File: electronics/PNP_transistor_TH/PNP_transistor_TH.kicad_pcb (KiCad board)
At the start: 2 copper layers, 19 x 19 mm, 7 parts, among them J1 B, J2 E, J3 C, J4 E, Q1 BC547

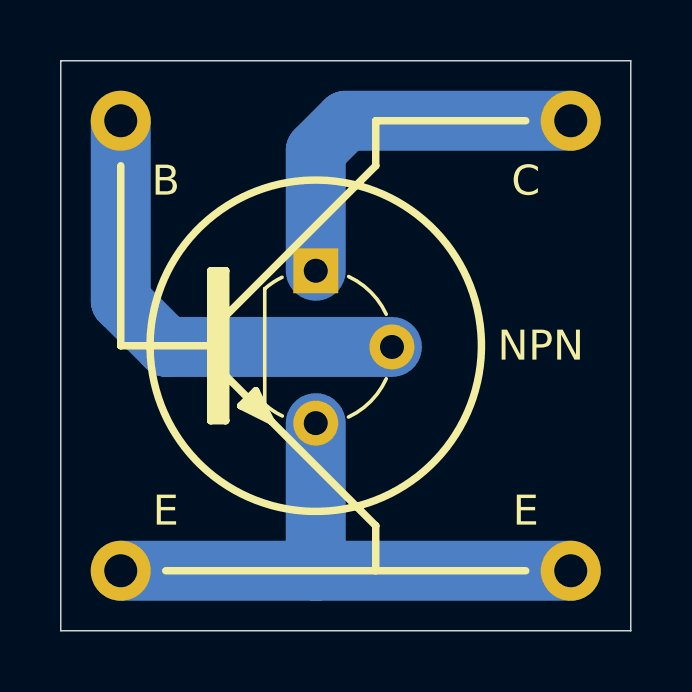
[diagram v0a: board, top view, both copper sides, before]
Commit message: final changes to PNP transistor
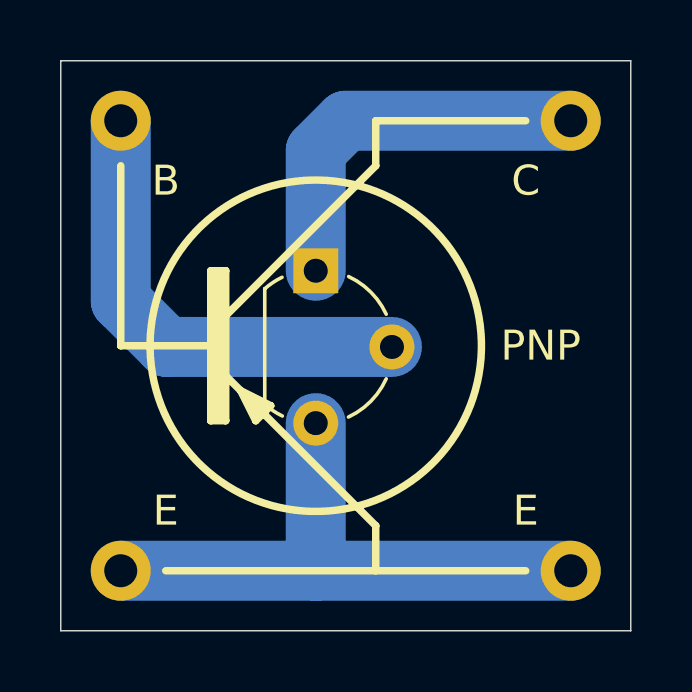
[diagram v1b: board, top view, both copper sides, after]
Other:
- board text added: "PNP"
- board text removed: "NPN"
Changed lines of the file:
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@@
   )
   (setup
-    (last_trace_width 2)
+    (last_trace_width 0.25)
     (user_trace_width 0.2)
     (user_trace_width 0.3)
@@
       (effects (font (size 1 1) (thickness 0.15)))
     )
+    (fp_line (start 0.65 1.6) (end 4.4 1.6) (layer F.Fab) (width 0.1))
+    (fp_line (start 0.6 1.7) (end 4.45 1.7) (layer F.SilkS) (width 0.12))
+    (fp_line (start -1 1.85) (end 6.1 1.85) (layer B.CrtYd) (width 0.05))
+    (fp_line (start 6.1 1.85) (end 6.1 -3.55) (layer B.CrtYd) (width 0.05))
+    (fp_line (start 6.1 -3.55) (end -1 -3.55) (layer B.CrtYd) (width 0.05))
+    (fp_line (start -1 -3.55) (end -1 1.85) (layer B.CrtYd) (width 0.05))
     (fp_arc (start 2.54 0) (end 4.45 1.7) (angle -15.88591585) (layer F.SilkS) (width 0.12))
     (fp_arc (start 2.54 0) (end 2.54 -2.48) (angle -130.2499344) (layer F.Fab) (width 0.1))
@@
       (effects (font (size 1 1) (thickness 0.15)))
     )
-    (fp_line (start -1 -3.55) (end -1 1.85) (layer B.CrtYd) (width 0.05))
-    (fp_line (start 6.1 -3.55) (end -1 -3.55) (layer B.CrtYd) (width 0.05))
-    (fp_line (start 6.1 1.85) (end 6.1 -3.55) (layer B.CrtYd) (width 0.05))
-    (fp_line (start -1 1.85) (end 6.1 1.85) (layer B.CrtYd) (width 0.05))
-    (fp_line (start 0.6 1.7) (end 4.45 1.7) (layer F.SilkS) (width 0.12))
-    (fp_line (start 0.65 1.6) (end 4.4 1.6) (layer F.Fab) (width 0.1))
     (pad 1 thru_hole rect (at 0 0 270) (size 1.5 1.5) (drill 0.8) (layers *.Cu *.Mask)
       (net 3 "Net-(J3-Pad1)"))
@@
       (effects (font (size 1 1) (thickness 0.15)))
     )
+    (fp_circle (center 0 0) (end 1.3 0) (layer F.CrtYd) (width 0.025))
     (fp_circle (center 0 0) (end 1.3 0) (layer B.CrtYd) (width 0.025))
-    (fp_circle (center 0 0) (end 1.3 0) (layer F.CrtYd) (width 0.025))
     (pad 1 thru_hole circle (at 0 0) (size 2 2) (drill 1.1) (layers *.Cu *.Mask)
       (net 2 "Net-(J2-Pad1)"))
@@
       (effects (font (size 1 1) (thickness 0.15)))
     )
+    (fp_circle (center 0 0) (end 1.3 0) (layer F.CrtYd) (width 0.025))
     (fp_circle (center 0 0) (end 1.3 0) (layer B.CrtYd) (width 0.025))
-    (fp_circle (center 0 0) (end 1.3 0) (layer F.CrtYd) (width 0.025))
     (pad 1 thru_hole circle (at 0 0) (size 2 2) (drill 1.1) (layers *.Cu *.Mask)
       (net 3 "Net-(J3-Pad1)"))
@@
       (effects (font (size 1 1) (thickness 0.15)))
     )
+    (fp_circle (center 0 0) (end 1.3 0) (layer F.CrtYd) (width 0.025))
     (fp_circle (center 0 0) (end 1.3 0) (layer B.CrtYd) (width 0.025))
-    (fp_circle (center 0 0) (end 1.3 0) (layer F.CrtYd) (width 0.025))
     (pad 1 thru_hole circle (at 0 0) (size 2 2) (drill 1.1) (layers *.Cu *.Mask)
       (net 2 "Net-(J2-Pad1)"))
@@
       (effects (font (size 1 1) (thickness 0.15)))
     )
+    (fp_circle (center 0 0) (end 1.3 0) (layer F.CrtYd) (width 0.025))
     (fp_circle (center 0 0) (end 1.3 0) (layer B.CrtYd) (width 0.025))
-    (fp_circle (center 0 0) (end 1.3 0) (layer F.CrtYd) (width 0.025))
     (pad 1 thru_hole circle (at 0 0) (size 2 2) (drill 1.1) (layers *.Cu *.Mask)
       (net 1 "Net-(J1-Pad1)"))
@@
     (fp_line (start -0.5 -0.6) (end 0.5 -0.6) (layer B.SilkS) (width 0.15))
   )
-  (gr_poly (pts (xy 147 73) (xy 146 72.5) (xy 146.5 72)) (layer F.SilkS) (width 0.1))
+  (gr_poly (pts (xy 147 72.5) (xy 146.5 73) (xy 146 72)) (layer F.SilkS) (width 0.1))
+  (gr_line (start 146.5 73) (end 146 72) (layer F.SilkS) (width 0.25))
+  (gr_line (start 147 72.5) (end 146.5 73) (layer F.SilkS) (width 0.25))
+  (gr_line (start 146 72) (end 147 72.5) (layer F.SilkS) (width 0.25))
   (gr_poly (pts (xy 145.5 73) (xy 145 73) (xy 145 68) (xy 145.5 68)) (layer F.SilkS) (width 0.1))
-  (gr_line (start 146 72.5) (end 147 73) (layer F.SilkS) (width 0.25))
-  (gr_line (start 146.5 72) (end 146 72.5) (layer F.SilkS) (width 0.25))
-  (gr_line (start 147 73) (end 146.5 72) (layer F.SilkS) (width 0.25))
   (gr_line (start 150.5 63) (end 155.5 63) (layer F.SilkS) (width 0.25))
   (gr_line (start 150.5 64.5) (end 150.5 63) (layer F.SilkS) (width 0.25))
@@
   (gr_line (start 142 70.5) (end 145 70.5) (layer F.SilkS) (width 0.25))
   (gr_line (start 142 64.5) (end 142 70.5) (layer F.SilkS) (width 0.25))
-  (gr_text NPN (at 156 70.5) (layer F.SilkS)
+  (gr_text PNP (at 156 70.5) (layer F.SilkS)
     (effects (font (size 1 1) (thickness 0.15)))
   )

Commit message: small fixes to PNP transistor module
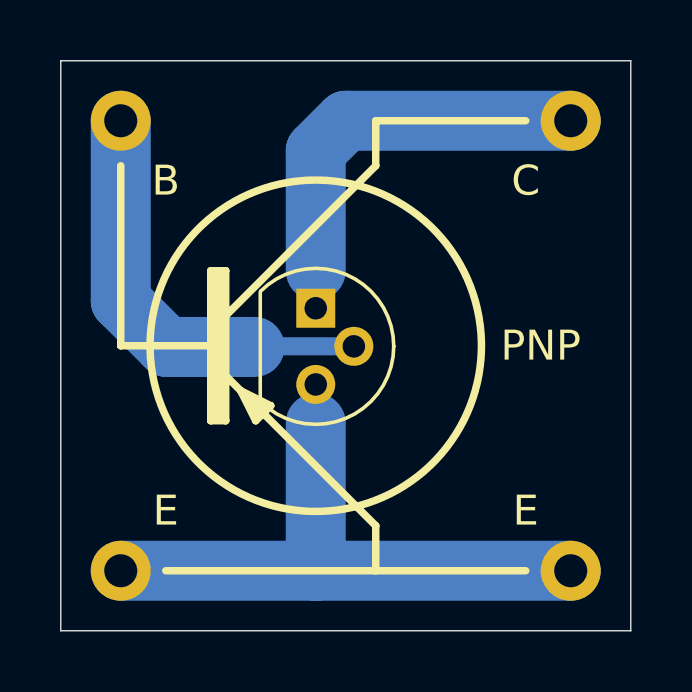
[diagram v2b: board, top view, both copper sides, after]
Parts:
- N1: value 20201118 -> V20201122
- Q1: footprint Package_TO_SOT_THT:TO-92L_Wide -> Package_TO_SOT_THT:TO-92
- moved N1 16.3 mm to (157.8, 71.2)
- moved N2 1.50 mm to (154.0, 70.5)
- moved Q1 1.25 mm to (148.5, 69.2)
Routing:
- net Net-(J2-Pad1): track 19.9 -> 21.2 mm
- net Net-(J1-Pad1): track 15.7 -> 14.4 mm
- net Net-(J3-Pad1): track 12.9 -> 14.2 mm
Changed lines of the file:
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@@
     (thickness 1.6)
     (drawings 24)
-    (tracks 9)
+    (tracks 13)
     (zones 0)
     (modules 7)
@@
   )
   (setup
-    (last_trace_width 0.25)
+    (last_trace_width 0.6)
     (user_trace_width 0.2)
     (user_trace_width 0.3)
@@
     (add_net "Net-(J3-Pad1)")
   )
-  (module Package_TO_SOT_THT:TO-92L_Wide (layer F.Cu)
-    (at 148.5 68 270)
-    (descr "TO-92L leads in-line (large body variant of TO-92), also known as TO-226, wide, drill 0.75mm (see https://www.diodes.com/assets/Package-Files/TO92L.pdf and http://www.ti.com/lit/an/snoa059/snoa059.pdf)")
-    (tags "TO-92L Molded Wide transistor")
-    (fp_text reference Q1 (at 2.55 -4.15 90) (layer F.Fab)
-      (effects (font (size 1 1) (thickness 0.15)))
-    )
-    (fp_text value BC547 (at 2.54 2.79 90) (layer F.Fab)
-      (effects (font (size 1 1) (thickness 0.15)))
-    )
-    (fp_line (start 0.65 1.6) (end 4.4 1.6) (layer F.Fab) (width 0.1))
-    (fp_line (start 0.6 1.7) (end 4.45 1.7) (layer F.SilkS) (width 0.12))
-    (fp_line (start -1 1.85) (end 6.1 1.85) (layer B.CrtYd) (width 0.05))
-    (fp_line (start 6.1 1.85) (end 6.1 -3.55) (layer B.CrtYd) (width 0.05))
-    (fp_line (start 6.1 -3.55) (end -1 -3.55) (layer B.CrtYd) (width 0.05))
-    (fp_line (start -1 -3.55) (end -1 1.85) (layer B.CrtYd) (width 0.05))
-    (fp_arc (start 2.54 0) (end 4.45 1.7) (angle -15.88591585) (layer F.SilkS) (width 0.12))
-    (fp_arc (start 2.54 0) (end 2.54 -2.48) (angle -130.2499344) (layer F.Fab) (width 0.1))
-    (fp_arc (start 2.54 0) (end 2.54 -2.48) (angle 129.9527847) (layer F.Fab) (width 0.1))
-    (fp_arc (start 2.54 0) (end 3.6 -2.35) (angle 40.72153779) (layer F.SilkS) (width 0.12))
-    (fp_arc (start 2.54 0) (end 1.45 -2.35) (angle -40.11670855) (layer F.SilkS) (width 0.12))
-    (fp_arc (start 2.54 0) (end 0.6 1.7) (angle 15.44288892) (layer F.SilkS) (width 0.12))
-    (fp_text user %R (at 2.54 0 90) (layer F.Fab)
-      (effects (font (size 1 1) (thickness 0.15)))
-    )
-    (pad 1 thru_hole rect (at 0 0 270) (size 1.5 1.5) (drill 0.8) (layers *.Cu *.Mask)
+  (module Package_TO_SOT_THT:TO-92 (layer F.Cu)
+    (at 148.5 69.25 270)
+    (descr "TO-92 leads molded, narrow, drill 0.75mm (see NXP sot054_po.pdf)")
+    (tags "to-92 sc-43 sc-43a sot54 PA33 transistor")
+    (fp_text reference Q1 (at 1.27 0 90) (layer F.Fab)
+      (effects (font (size 1 1) (thickness 0.15)))
+    )
+    (fp_text value BC547 (at 1.27 2.79 90) (layer F.Fab)
+      (effects (font (size 1 1) (thickness 0.15)))
+    )
+    (fp_arc (start 1.27 0) (end 1.27 -2.6) (angle 135) (layer F.SilkS) (width 0.12))
+    (fp_arc (start 1.27 0) (end 1.27 -2.48) (angle -135) (layer F.Fab) (width 0.1))
+    (fp_arc (start 1.27 0) (end 1.27 -2.6) (angle -135) (layer F.SilkS) (width 0.12))
+    (fp_arc (start 1.27 0) (end 1.27 -2.48) (angle 135) (layer F.Fab) (width 0.1))
+    (fp_text user %R (at 1.27 0 90) (layer F.Fab)
+      (effects (font (size 1 1) (thickness 0.15)))
+    )
+    (fp_line (start -0.53 1.85) (end 3.07 1.85) (layer F.SilkS) (width 0.12))
+    (fp_line (start -0.5 1.75) (end 3 1.75) (layer F.Fab) (width 0.1))
+    (fp_line (start -1.46 -2.73) (end 4 -2.73) (layer F.CrtYd) (width 0.05))
+    (fp_line (start -1.46 -2.73) (end -1.46 2.01) (layer F.CrtYd) (width 0.05))
+    (fp_line (start 4 2.01) (end 4 -2.73) (layer F.CrtYd) (width 0.05))
+    (fp_line (start 4 2.01) (end -1.46 2.01) (layer F.CrtYd) (width 0.05))
+    (pad 1 thru_hole rect (at 0 0 270) (size 1.3 1.3) (drill 0.75) (layers *.Cu *.Mask)
       (net 3 "Net-(J3-Pad1)"))
-    (pad 3 thru_hole circle (at 5.08 0 270) (size 1.5 1.5) (drill 0.8) (layers *.Cu *.Mask)
+    (pad 3 thru_hole circle (at 2.54 0 270) (size 1.3 1.3) (drill 0.75) (layers *.Cu *.Mask)
       (net 2 "Net-(J2-Pad1)"))
-    (pad 2 thru_hole circle (at 2.54 -2.54 270) (size 1.5 1.5) (drill 0.8) (layers *.Cu *.Mask)
+    (pad 2 thru_hole circle (at 1.27 -1.27 270) (size 1.3 1.3) (drill 0.75) (layers *.Cu *.Mask)
       (net 1 "Net-(J1-Pad1)"))
-    (model ${KISYS3DMOD}/Package_TO_SOT_THT.3dshapes/TO-92L_Wide.wrl
+    (model ${KISYS3DMOD}/Package_TO_SOT_THT.3dshapes/TO-92.wrl
       (at (xyz 0 0 0))
       (scale (xyz 1 1 1))
@@
       (effects (font (size 1 1) (thickness 0.15)))
     )
+    (fp_circle (center 0 0) (end 1.3 0) (layer B.CrtYd) (width 0.025))
     (fp_circle (center 0 0) (end 1.3 0) (layer F.CrtYd) (width 0.025))
-    (fp_circle (center 0 0) (end 1.3 0) (layer B.CrtYd) (width 0.025))
     (pad 1 thru_hole circle (at 0 0) (size 2 2) (drill 1.1) (layers *.Cu *.Mask)
       (net 2 "Net-(J2-Pad1)"))
@@
       (effects (font (size 1 1) (thickness 0.15)))
     )
+    (fp_circle (center 0 0) (end 1.3 0) (layer B.CrtYd) (width 0.025))
     (fp_circle (center 0 0) (end 1.3 0) (layer F.CrtYd) (width 0.025))
-    (fp_circle (center 0 0) (end 1.3 0) (layer B.CrtYd) (width 0.025))
     (pad 1 thru_hole circle (at 0 0) (size 2 2) (drill 1.1) (layers *.Cu *.Mask)
       (net 3 "Net-(J3-Pad1)"))
@@
       (effects (font (size 1 1) (thickness 0.15)))
     )
+    (fp_circle (center 0 0) (end 1.3 0) (layer B.CrtYd) (width 0.025))
     (fp_circle (center 0 0) (end 1.3 0) (layer F.CrtYd) (width 0.025))
-    (fp_circle (center 0 0) (end 1.3 0) (layer B.CrtYd) (width 0.025))
     (pad 1 thru_hole circle (at 0 0) (size 2 2) (drill 1.1) (layers *.Cu *.Mask)
       (net 2 "Net-(J2-Pad1)"))
@@
       (effects (font (size 1 1) (thickness 0.15)))
     )
+    (fp_circle (center 0 0) (end 1.3 0) (layer B.CrtYd) (width 0.025))
     (fp_circle (center 0 0) (end 1.3 0) (layer F.CrtYd) (width 0.025))
-    (fp_circle (center 0 0) (end 1.3 0) (layer B.CrtYd) (width 0.025))
     (pad 1 thru_hole circle (at 0 0) (size 2 2) (drill 1.1) (layers *.Cu *.Mask)
       (net 1 "Net-(J1-Pad1)"))
   )
   (module Symbol:OSHW-Symbol_6.7x6mm_SilkScreen (layer B.Cu)
-    (at 155.5 70.5 270)
+    (at 154 70.5 270)
     (descr "Open Source Hardware Symbol")
     (tags "Logo Symbol OSHW")
@@
   )
   (module SquantorLabels:Label_Generic (layer B.Cu)
-    (at 141.5 71.5 90)
+    (at 157.75 71.25 90)
     (descr "Label for general purpose use")
     (tags Label)
@@
       (effects (font (size 1 1) (thickness 0.15)) (justify mirror))
     )
-    (fp_text value 20201118 (at 0.8 0.1 90) (layer B.SilkS)
+    (fp_text value V20201122 (at 0.8 0.1 90) (layer B.SilkS)
       (effects (font (size 0.8 0.8) (thickness 0.15)) (justify mirror))
     )
@@
   (gr_line (start 140 80) (end 159 80) (layer Edge.Cuts) (width 0.05))
   (gr_line (start 140 80) (end 140 61) (layer Edge.Cuts) (width 0.05))
-  (segment (start 151.04 70.54) (end 143.54 70.54) (width 2) (layer B.Cu) (net 1))
   (segment (start 142 69) (end 142 63) (width 2) (layer B.Cu) (net 1))
   (segment (start 143.54 70.54) (end 142 69) (width 2) (layer B.Cu) (net 1))
+  (segment (start 143.54 70.54) (end 146.46 70.54) (width 2) (layer B.Cu) (net 1))
+  (segment (start 146.48 70.52) (end 146.46 70.54) (width 0.6) (layer B.Cu) (net 1))
+  (segment (start 149.77 70.52) (end 146.48 70.52) (width 0.6) (layer B.Cu) (net 1))
   (segment (start 148.5 73.08) (end 148.5 78) (width 2) (layer B.Cu) (net 2))
   (segment (start 148.5 78) (end 157 78) (width 2) (layer B.Cu) (net 2))
   (segment (start 142 78) (end 148.5 78) (width 2) (layer B.Cu) (net 2))
+  (segment (start 148.5 73.08) (end 148.5 71.79) (width 0.6) (layer B.Cu) (net 2))
   (segment (start 148.5 68) (end 148.5 64) (width 2) (layer B.Cu) (net 3))
   (segment (start 149.5 63) (end 157 63) (width 2) (layer B.Cu) (net 3))
   (segment (start 148.5 64) (end 149.5 63) (width 2) (layer B.Cu) (net 3))
+  (segment (start 148.5 69.25) (end 148.5 68) (width 0.6) (layer B.Cu) (net 3))
 )
